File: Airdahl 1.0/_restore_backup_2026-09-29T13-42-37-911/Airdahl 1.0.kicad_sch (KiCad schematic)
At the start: 71 parts, among them J1 Conn_01x04, J2 DF40C-34DS-0.4V_58_, J3 DF40C-34DS-0.4V_58_, J4 USB_C_Receptacle_USB2.0_16P, SW1 SW_SPST, SW2 SW_SPST, U1 STM32F446RETx, U2 MCP2200-I-MQ, U3 LM66200DRLR, U7 NCP1117-3.3_SOT223, U8 LM66200DRLR, Y1 ABM3B-8.000MHZ-12-D1X-T, Y2 ABS25-32.768KHZ-6-T, Y3 12MHz

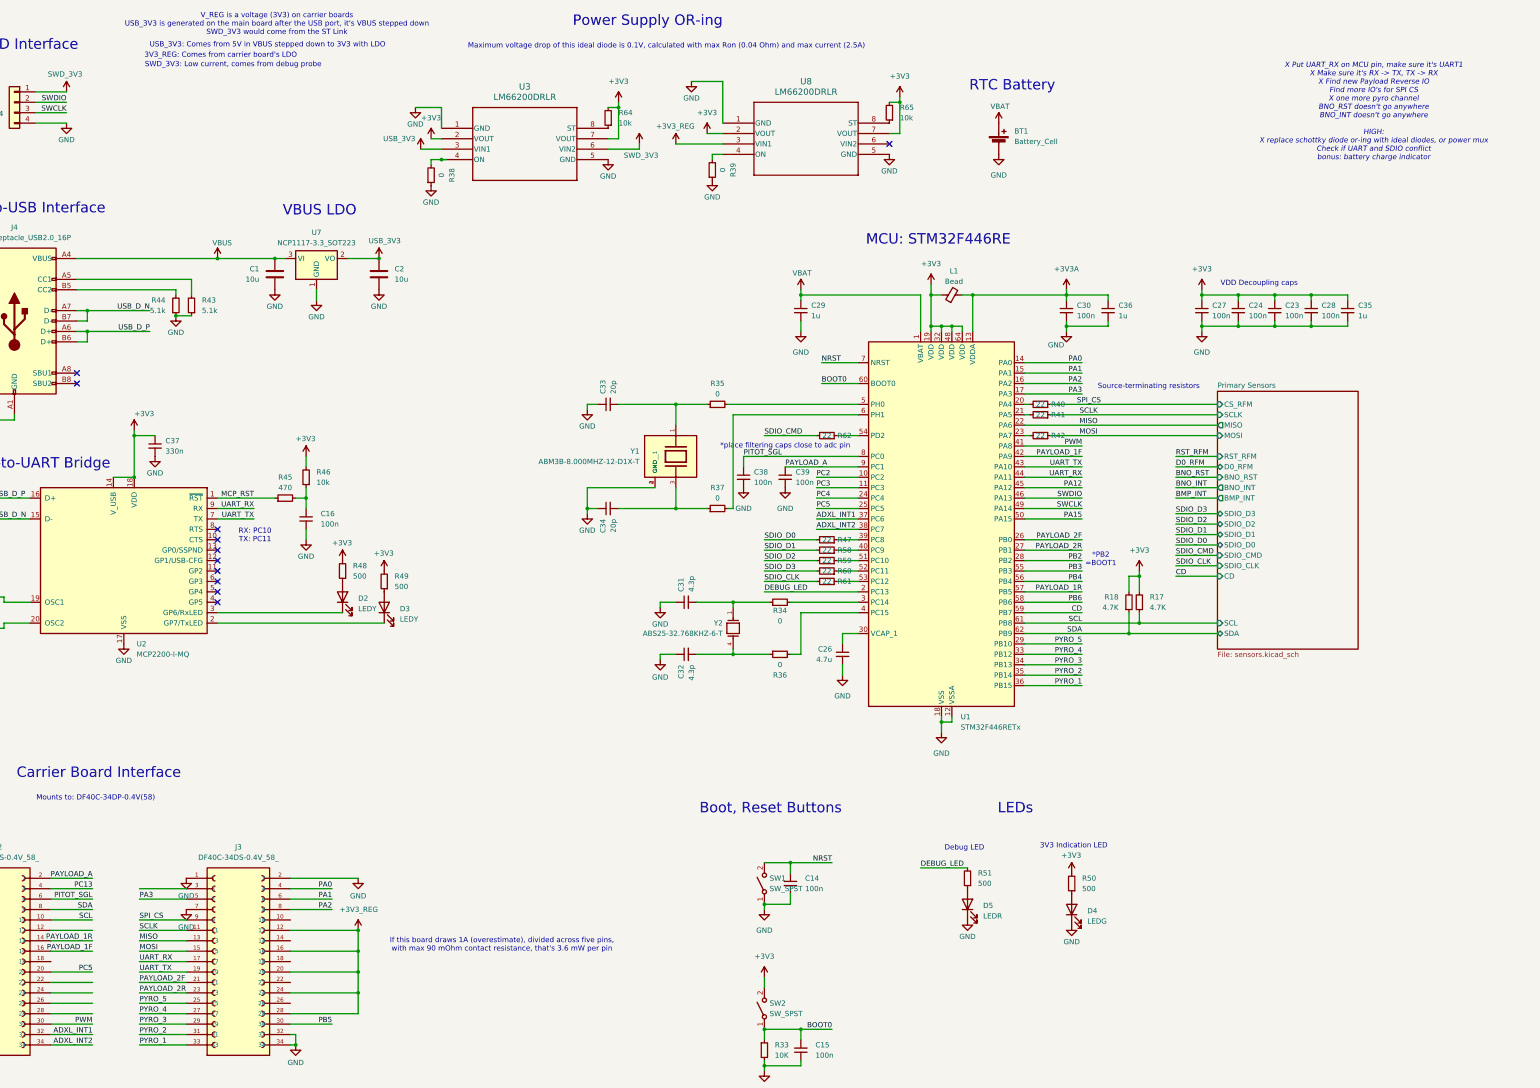
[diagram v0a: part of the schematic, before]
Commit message: power or-ing changes
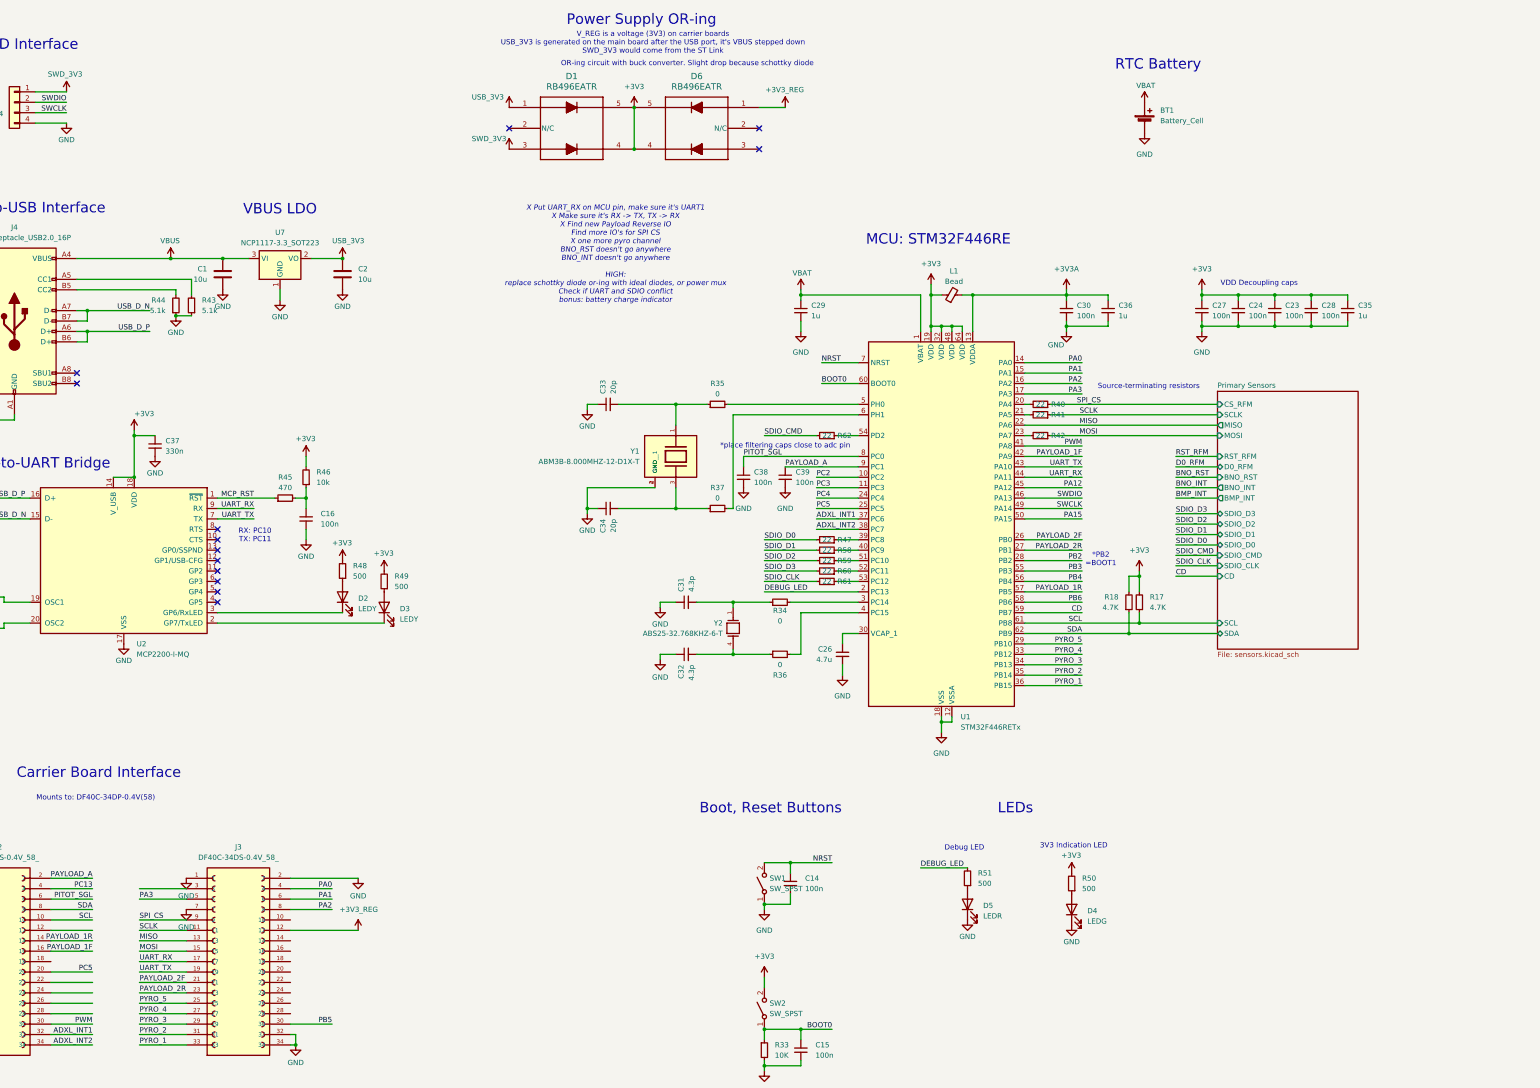
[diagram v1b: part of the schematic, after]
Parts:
- removed R38, R39: 0, Resistor_SMD:R_0402_1005Metric, symbol Device:R_Small
- removed R64, R65: 10k, Resistor_SMD:R_0402_1005Metric, symbol Device:R_Small
- removed U3, U8: LM66200DRLR, SOT-5X3_DRL_TEX, symbol LM66200DRLR:LM66200DRLR
- added D1, D6: RB496EATR, DIO_FTZ_ROM, symbol RB496EATR:RB496EATR
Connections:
- net +3V3: now also D1.4, D1.5, D6.4, D6.5
- net +3V3_REG: now also D6.1; no longer J3.16, J3.20, J3.24, J3.28
- net SWD_3V3: now also D1.3
- net USB_3V3: now also D1.1
- no-connect marks 11 -> 13
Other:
- note added: "OR-ing circuit with buck converter. Slight drop because schottky diode"
- note added: "X Put UART_RX on MCU pin, make sure it's UART1 X Make sure it's RX -> TX, TX -> RX X Find new Payload Reverse IO Find more IO's for SPI CS X one more pyro channel BNO_RST doesn't go anywhere BNO_INT doesn't go anywhere HIGH: replace schottky diode or-ing with ideal diodes, or power mux Check if UART and SDIO conflict bonus: battery charge indicator"
- note removed: "3V3_REG: Comes from carrier board's LDO"
- note removed: "If this board draws 1A (overestimate), divided across five pins, with max 90 mOhm contact resistance, that's 3.6 mW per pin"
- note removed: "Maximum voltage drop of this ideal diode is 0.1V, calculated with max Ron (0.04 Ohm) and max current (2.5A)"
- note removed: "SWD_3V3: Low current, comes from debug probe"
- note removed: "USB_3V3: Comes from 5V in VBUS stepped down to 3V3 with LDO"
- note removed: "X Put UART_RX on MCU pin, make sure it's UART1 X Make sure it's RX -> TX, TX -> RX X Find new Payload Reverse IO Find more IO's for SPI CS X one more pyro channel BNO_RST doesn't go anywhere BNO_INT doesn't go anywhere HIGH: X replace schottky diode or-ing with ideal diodes, or power mux Check if UART and SDIO conflict bonus: battery charge indicator"
- moved on the sheet: BT1
